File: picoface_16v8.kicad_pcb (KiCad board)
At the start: 2 copper layers, 79.2 x 69.6 mm, 23 parts, among them J1 ZX_Spectrum_Connector_48K_SOR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, J2 DE9_Plug, Q1 DMG2305, SW1 SW_USER, SW2 SW_RESET, SW3 SW_RUN, U2 Pico, U3 74LS240

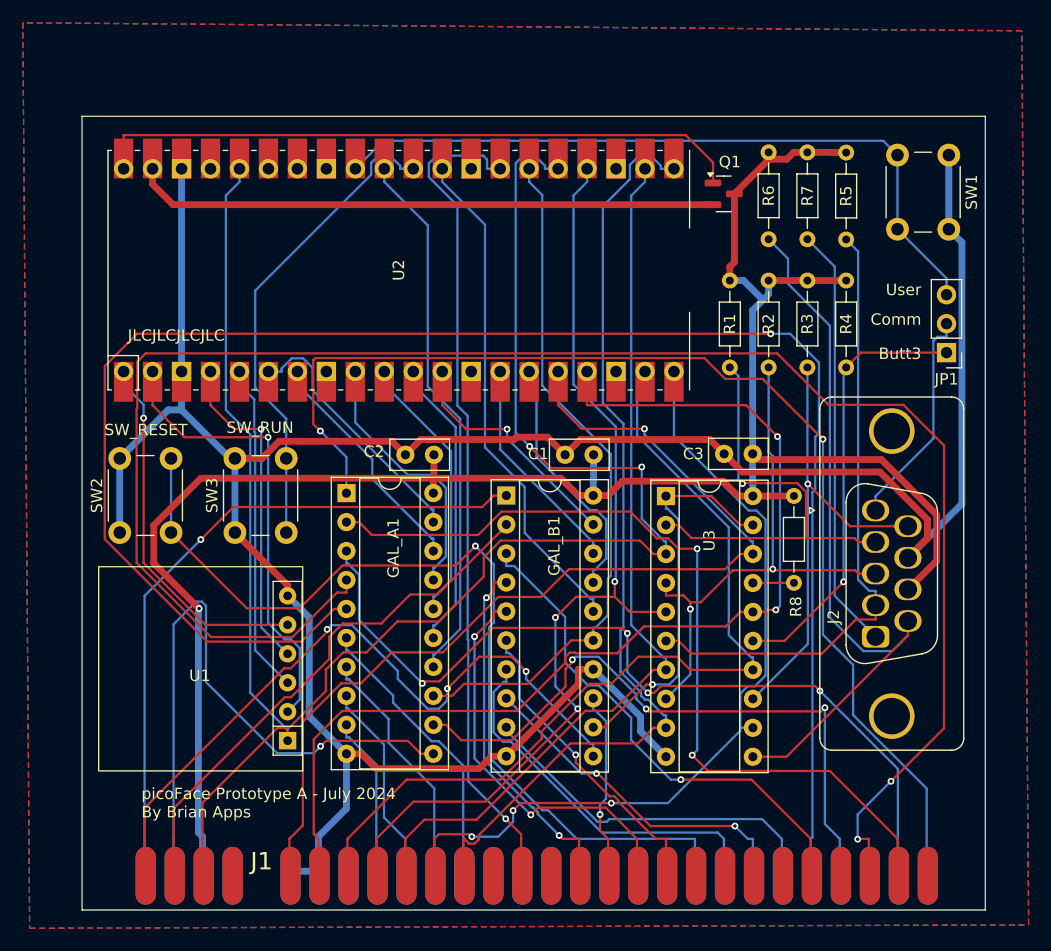
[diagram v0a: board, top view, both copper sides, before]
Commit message: Prototype B board, fix up mistakes in prototype A
Correct the joystick up connection, make SD card drill holes slightly larger.
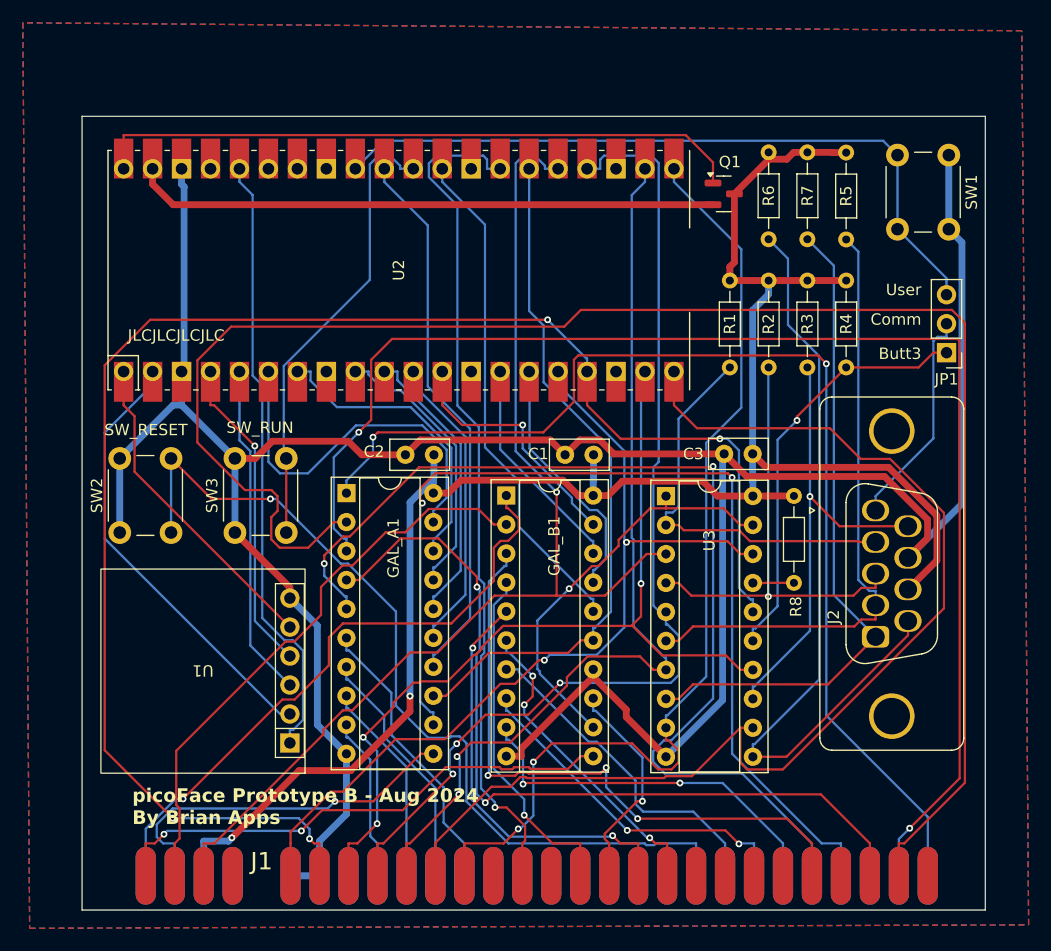
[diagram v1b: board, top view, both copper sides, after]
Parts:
- moved U1 0.28 mm to (127.6, 93.6)
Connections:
- U3 pad 8: /J_LEFT -> /J_UP
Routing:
- net /A8: track 157.3 -> 73.3 mm
- net /A10: track 75.6 -> 148.8 mm, vias 2 -> 0
- net /A4: track 151.0 -> 91.1 mm, vias 1 -> 2
- net /A9: track 74.8 -> 120.3 mm, vias 4 -> 2
- net /D1: track 93.5 -> 138.6 mm, vias 2 -> 4
- net /~{CSROM}: track 56.2 -> 89.4 mm, vias 3 -> 2
- net /D3: track 72.0 -> 100.9 mm, vias 3 -> 0
- net /A12: track 55.6 -> 32.6 mm
- net /J_UP: track 37.3 -> 58.0 mm
- net /A15: track 62.3 -> 45.5 mm, vias 3 -> 2
- net /GND: track 230.3 -> 243.6 mm
- net /M1: track 44.0 -> 55.6 mm, vias 1 -> 3
- net /VCC: track 174.2 -> 163.0 mm, vias 1 -> 2
- net /A0xA8: track 22.8 -> 33.5 mm
- net /D7: track 107.9 -> 98.2 mm, vias 2 -> 1
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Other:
- board text added: "picoFace Prototype B - Aug 2024 By Brian Apps"
- board text removed: "picoFace Prototype A - July 2024 By Brian Apps"

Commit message: Prototype B with pico ultimate pinout
Has two set of pads for the different types of pico.
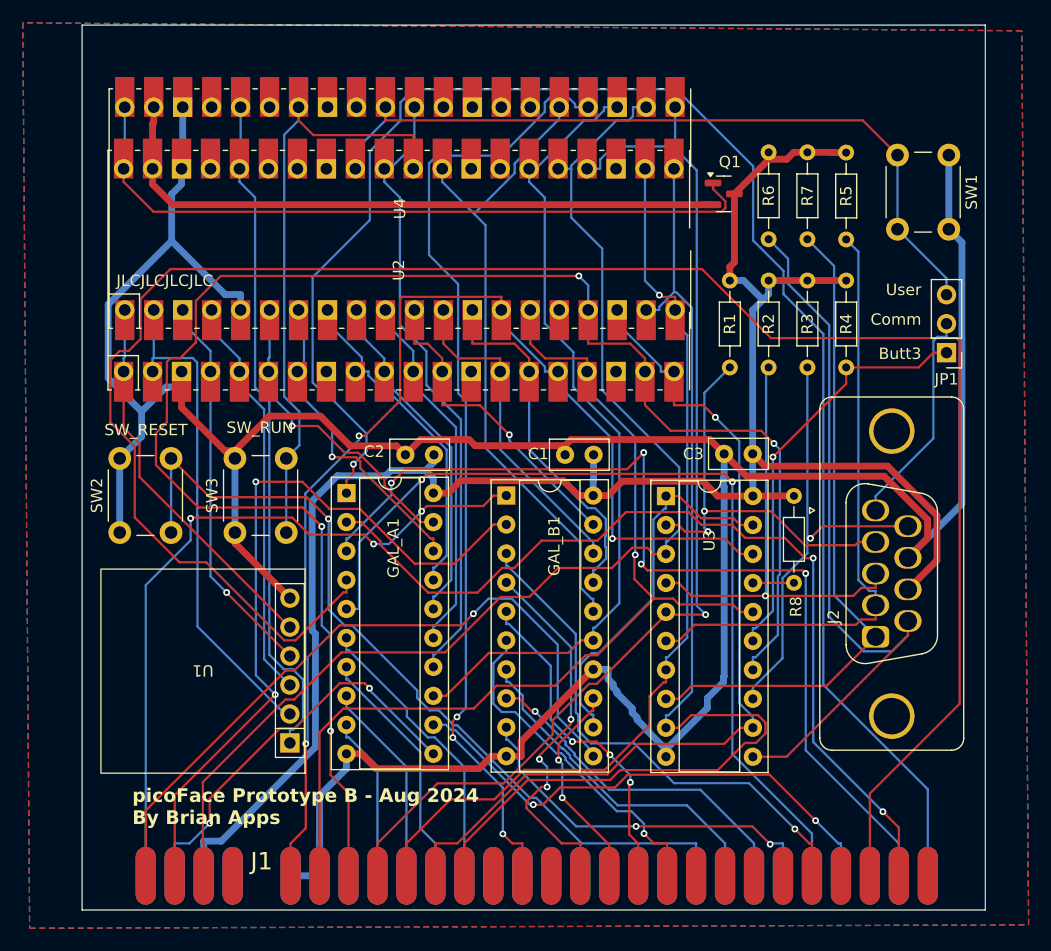
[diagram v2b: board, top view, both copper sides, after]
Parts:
- added U4: Pico, mysyms:RPi_Pico_SMD_TH_BA2, F.Cu at (144.9, 53.1)
- U2: footprint mysyms:RPi_Pico_SMD_TH_BA -> mysyms:RPi_Pico_SMD_TH_BA2
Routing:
- net /A8: track 73.3 -> 173.1 mm, vias 2 -> 0
- net /D2: track 77.0 -> 149.0 mm, vias 3 -> 4
- net /A10: track 148.8 -> 79.2 mm, vias 0 -> 2
- net /D1: track 138.6 -> 87.9 mm, vias 4 -> 1
- net /~{CSROM}: track 89.4 -> 45.1 mm
- net /A11: track 99.6 -> 143.1 mm, vias 2 -> 1
- net /A9: track 120.3 -> 85.4 mm, vias 2 -> 4
- net /GND: track 243.6 -> 271.3 mm
- net /D0: track 77.2 -> 102.8 mm, vias 2 -> 3
- net /D3: track 100.9 -> 78.7 mm, vias 0 -> 1
- net /A15: track 45.5 -> 62.3 mm, vias 2 -> 1
- net /A13: track 51.0 -> 65.3 mm, vias 0 -> 2
- net /RUN: track 40.3 -> 53.6 mm
- net /~{PICOREQ}: track 44.4 -> 56.9 mm
- net /~{NMI}: track 74.4 -> 86.1 mm, vias 1 -> 3
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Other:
- board size 79.2 x 69.6 mm -> 79.2 x 77.6 mm
